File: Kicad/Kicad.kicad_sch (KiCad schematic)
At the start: 6 parts, among them J1 Screw_Terminal_01x02, J2 Screw_Terminal_01x02, J3 Screw_Terminal_01x04, U1 ESP32-WROOM-32, U2 DRV8833PW

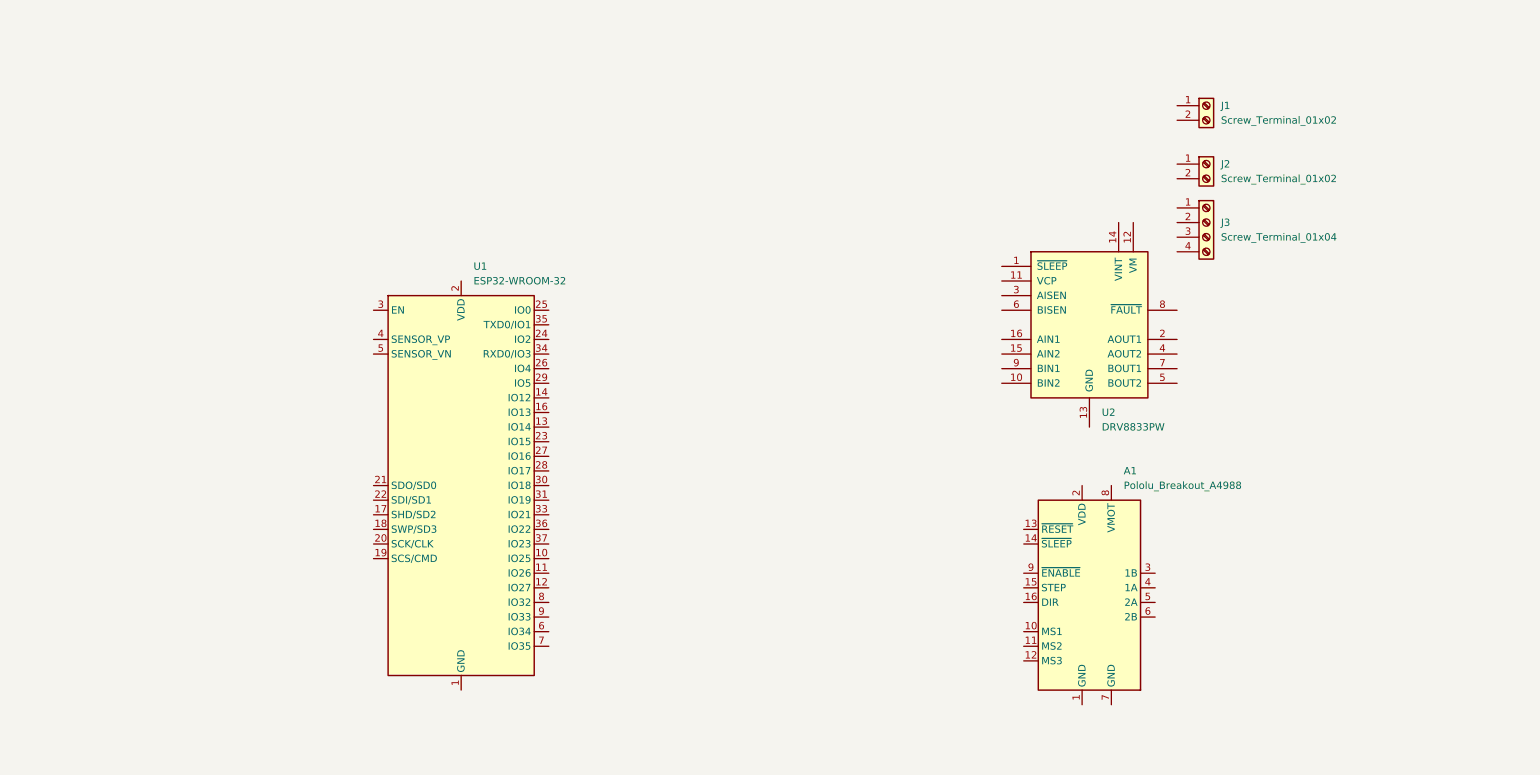
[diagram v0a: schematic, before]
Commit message: Added Power Board
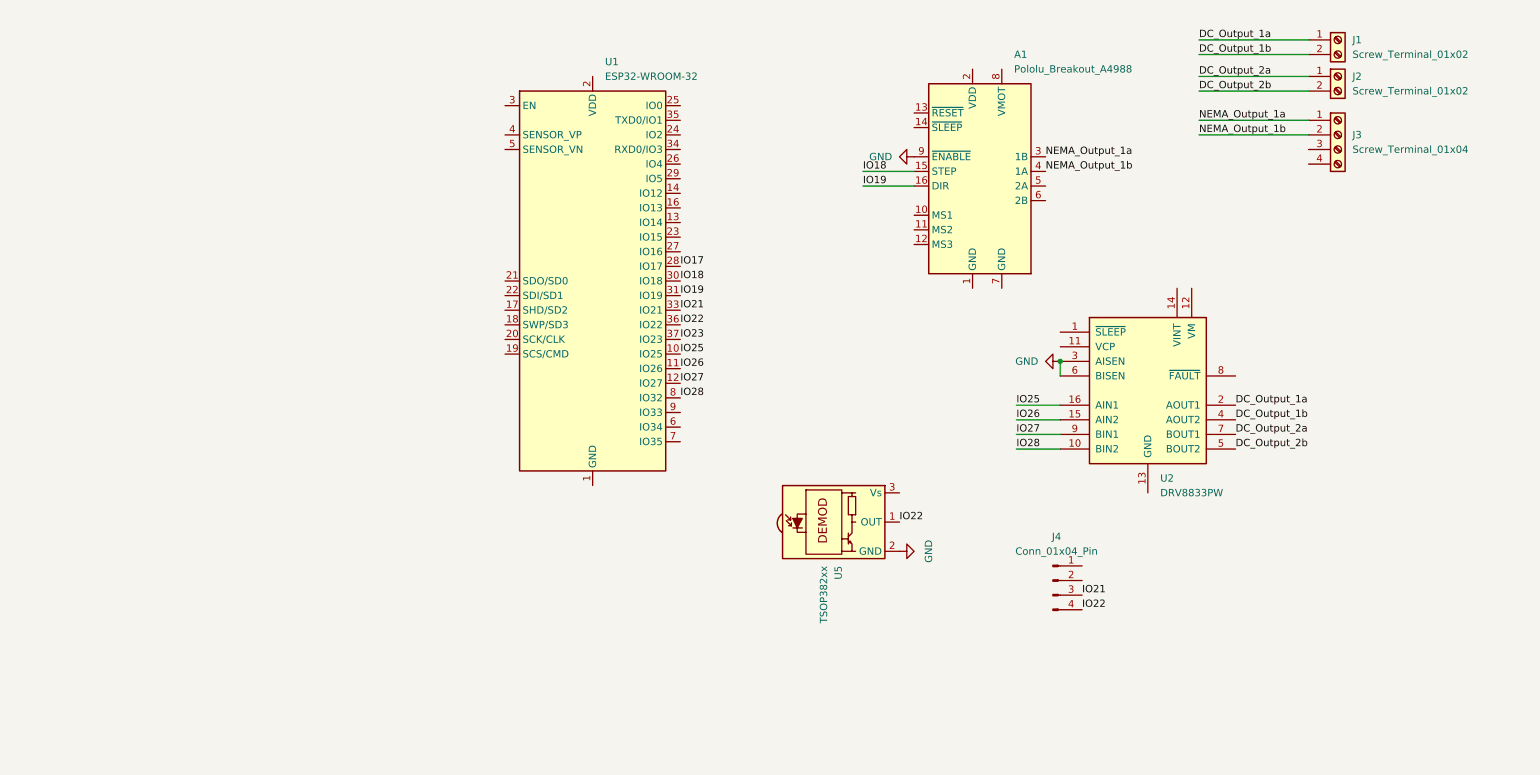
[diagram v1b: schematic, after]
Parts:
- added J4: Conn_01x04_Pin, Connector_PinHeader_2.54mm:PinHeader_1x04_P2.54mm_Vertical, symbol Connector:Conn_01x04_Pin
- added U5: TSOP382xx, OptoDevice:Vishay_MINICAST-3Pin, symbol Interface_Optical:TSOP382xx
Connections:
- net DC_Output_1a: now reaches J1.1 (Pin_1)
- net DC_Output_1a: now also U2.2 (AOUT1)
- net DC_Output_1b: now reaches J1.2 (Pin_2)
- net DC_Output_1b: now also U2.4 (AOUT2)
- net IO25: now reaches U1.10 (IO25)
- net IO25: now also U2.16 (AIN1)
- net IO26: now reaches U1.11 (IO26)
- net IO26: now also U2.15 (AIN2)
- net IO27: now reaches U1.12 (IO27)
- net IO27: now also U2.9 (BIN1)
- net IO17: now reaches U1.28 (IO17)
- net IO18: now reaches U1.30 (IO18)
- net IO18: now also A1.15 (STEP)
- net IO19: now reaches U1.31 (IO19)
- net IO19: now also A1.16 (DIR)
- net IO21: now reaches U1.33 (IO21)
- net IO21: now also J4.3 (Pin_3)
- net IO22: now reaches U1.36 (IO22)
- net IO22: now also J4.4 (Pin_4), U5.1 (OUT)
- net IO23: now reaches U1.37 (IO23)
- net IO28: now reaches U1.8 (IO32)
- net IO28: now also U2.10 (BIN2)
- net NEMA_Output_1a: now reaches A1.3 (1B)
- net NEMA_Output_1a: now also J3.1 (Pin_1)
- net NEMA_Output_1b: now reaches A1.4 (1A)
- net NEMA_Output_1b: now also J3.2 (Pin_2)
- net GND: now reaches A1.9 (~{ENABLE})
- net GND: now also U2.3 (AISEN), U2.6 (BISEN), U5.2 (GND)
- net DC_Output_2b: now reaches U2.5 (BOUT2)
- net DC_Output_2b: now also J2.2 (Pin_2)
- net DC_Output_2a: now reaches U2.7 (BOUT1)
- net DC_Output_2a: now also J2.1 (Pin_1)
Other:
- moved on the sheet: A1, J1, J2, J3, U1, U2

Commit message: Updated schematic for main board
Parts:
- added C1, C5: 10u, Capacitor_SMD:C_0603_1608Metric, symbol Device:C
- added C2, C3: 0.1u, Capacitor_SMD:C_0603_1608Metric, symbol Device:C
- added C4: 100u, Capacitor_SMD:C_0603_1608Metric, symbol Device:C
- added C6: 0.01u, Capacitor_SMD:C_0603_1608Metric, symbol Device:C
- added C7: 2.2u, Capacitor_SMD:C_0603_1608Metric, symbol Device:C
- added J5: Conn_01x04_Pin, Connector_PinHeader_2.54mm:PinHeader_1x04_P2.54mm_Vertical, symbol Connector:Conn_01x04_Pin
- added R1: 10k, Resistor_SMD:R_0603_1608Metric, symbol Device:R
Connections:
- net GND: now also A1.1 (GND), A1.7 (GND), J4.2 (Pin_2), U1.1 (GND), U1.15 (GND), U1.38 (GND), U1.39 (GND), U2.13 (GND), C1.1, C2.1, C3.1, C4.1, C5.1, C6.1, C7.1, J5.2 (Pin_2), J5.3 (Pin_3); no longer A1.9 (~{ENABLE})
- net IO23: now also A1.9 (~{ENABLE})
- net 3v3: now reaches U1.2 (VDD)
- net 3v3: now also A1.2 (VDD), J4.1 (Pin_1), U2.1 (~{SLEEP}), U2.11 (VCP), U2.12 (VM), U5.3 (Vs), C1.2, C2.2, C5.2, C6.2, J5.1 (Pin_1), R1.1
- net at U1.3 (EN): now also C3.2, R1.2
- net at A1.13 (~{RESET}): now also A1.14 (~{SLEEP})
- net NEMA_Output_2a: now reaches A1.5 (2A)
- net NEMA_Output_2a: now also J3.3 (Pin_3)
- net NEMA_Output_2b: now reaches A1.6 (2B)
- net NEMA_Output_2b: now also J3.4 (Pin_4)
- net 12V: now reaches A1.8 (VMOT)
- net 12V: now also C4.2, J5.4 (Pin_4)
- net at U2.14 (VINT): now also C7.2
- net IO17: no longer names the net of U1.28 (IO17)
- no-connect marks 0 -> 27
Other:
- moved on the sheet: U1

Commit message: Main Board v1
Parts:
- removed U1: ESP32-WROOM-32, RF_Module:ESP32-WROOM-32, symbol RF_Module:ESP32-WROOM-32
- added U3: ~, ESP32_Footprints:ESP32_30pin, symbol esp32_30pin:ESP32_30Pin
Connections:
- net 3v3: now also U3.16 (3.3v)
- net GND: now also C3.2, U3.17 (GND), U3.2 (GND); no longer C3.1
- net IO18: now also U3.3 (GPIO13)
- net IO19: now also U3.4 (GPIO12)
- net IO21: now also U3.29 (GPIO22)
- net IO22: now also U3.30 (GPIO23); no longer U5.1 (OUT)
- net IO23: now also U3.7 (GPIO26)
- net IO25: now also U2.9 (BIN1), U3.8 (GPIO25); no longer U2.16 (AIN1)
- net IO26: now also U2.10 (BIN2), U3.9 (GPIO33); no longer U2.15 (AIN2)
- net IO27: now also U2.15 (AIN2), U3.10 (GPIO32); no longer U2.9 (BIN1)
- net IO28: now also U2.16 (AIN1), U3.11 (GPIO35); no longer U2.10 (BIN2)
- net EN: now reaches R1.2
- net EN: now also C3.1, U3.15 (EN); no longer C3.2
- new net IO5: U3.23 (GPIO5), U5.1 (OUT)
- no-connect marks 27 -> 20
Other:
- moved on the sheet: C1, C2, C3, C5, C6, J5, R1

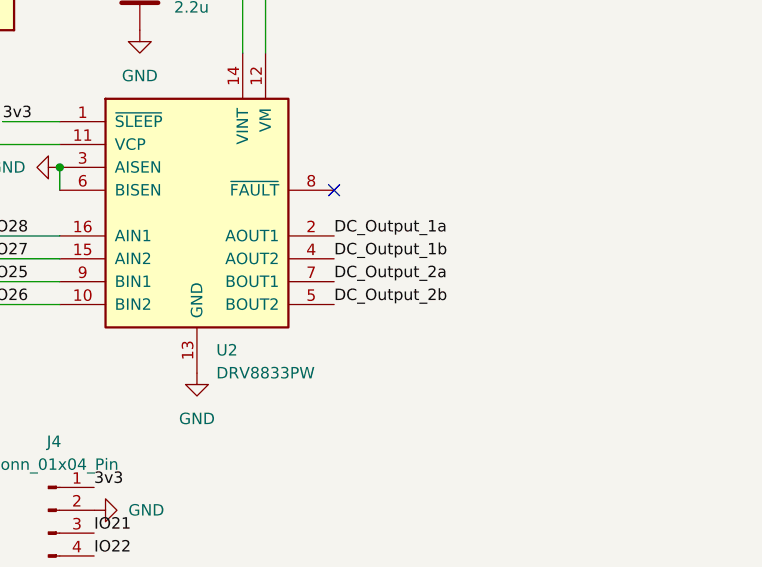
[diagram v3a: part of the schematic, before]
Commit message: Created cad for how the boards will fit together
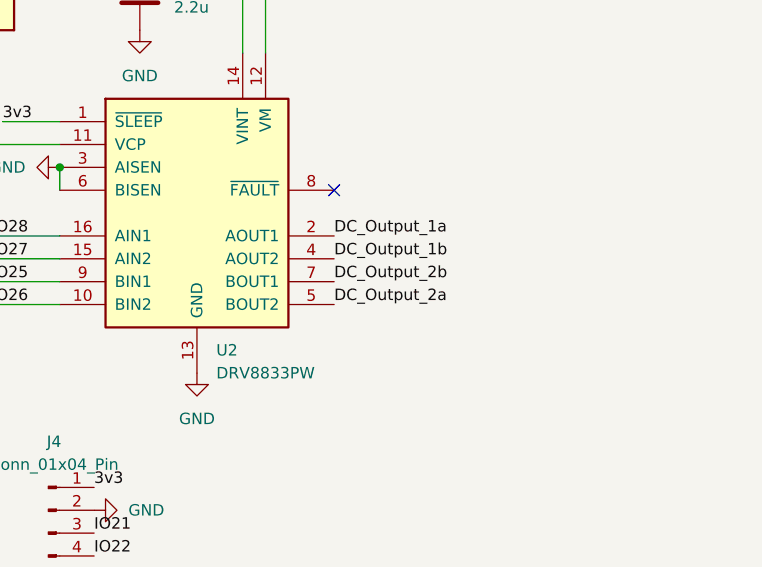
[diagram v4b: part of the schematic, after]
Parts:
- J1, J2: footprint TerminalBlock_RND:TerminalBlock_RND_205-00232_1x02_P5.08mm_Horizontal -> TerminalBlock_RND:TerminalBlock_RND_205-00045_1x02_P5.00mm_Horizontal
- J3: footprint TerminalBlock_Phoenix:TerminalBlock_Phoenix_MKDS-3-4-5.08_1x04_P5.08mm_Horizontal -> TerminalBlock_RND:TerminalBlock_RND_205-00003_1x04_P5.00mm_Horizontal
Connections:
- net DC_Output_2a: now also U2.5 (BOUT2); no longer U2.7 (BOUT1)
- net DC_Output_2b: now also U2.7 (BOUT1); no longer U2.5 (BOUT2)
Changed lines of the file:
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@@
+		)
+	)
+	(label "DC_Output_2b"
+		(at 234.95 95.25 0)
+		(effects
+			(font
+				(size 1.27 1.27)
+			)
+			(justify left bottom)
 		)
 	)
@@
 		)
 	)
-	(label "DC_Output_2b"
-		(at 234.95 97.79 0)
-		(effects
-			(font
-				(size 1.27 1.27)
-			)
-			(justify left bottom)
-		)
-	)
 	(label "3v3"
 		(at 198.12 77.47 0)
@@
 		)
 	)
-	(label "DC_Output_2a"
-		(at 234.95 95.25 0)
-		(effects
-			(font
-				(size 1.27 1.27)
-			)
-			(justify left bottom)
-		)
-	)
 	(label "IO5"
 		(at 176.53 110.49 0)
@@
 		)
 	)
+	(label "DC_Output_2a"
+		(at 234.95 97.79 0)
+		(effects
+			(font
+				(size 1.27 1.27)
+			)
+			(justify left bottom)
+		)
+	)
 	(label "3v3"
 		(at 87.63 43.18 0)
@@
 			)
 		)
-		(property "Footprint" "TerminalBlock_RND:TerminalBlock_RND_205-00232_1x02_P5.08mm_Horizontal"
+		(property "Footprint" "TerminalBlock_RND:TerminalBlock_RND_205-00045_1x02_P5.00mm_Horizontal"
 			(at 252.73 26.67 0)
 			(effects
@@
 			)
 		)
-		(property "Footprint" "TerminalBlock_RND:TerminalBlock_RND_205-00232_1x02_P5.08mm_Horizontal"
+		(property "Footprint" "TerminalBlock_RND:TerminalBlock_RND_205-00045_1x02_P5.00mm_Horizontal"
 			(at 252.73 33.02 0)
 			(effects
@@
 			)
 		)
-		(property "Footprint" "TerminalBlock_Phoenix:TerminalBlock_Phoenix_MKDS-3-4-5.08_1x04_P5.08mm_Horizontal"
+		(property "Footprint" "TerminalBlock_RND:TerminalBlock_RND_205-00003_1x04_P5.00mm_Horizontal"
 			(at 252.73 43.18 0)
 			(effects

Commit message: Wrote v1 of the code, final version of boards
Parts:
- C1, C5: value 10u -> 10uF; footprint Capacitor_SMD:C_0603_1608Metric -> PCM_JLCPCB:C_0603; symbol Device:C -> PCM_JLCPCB-Capacitors:0603,10uF; Attrition Qty (none) -> 10; Capacitance (none) -> 10uF; Category (none) -> Capacitors,Multilayer Ceramic Capacitors MLCC - SMD/SMT; Class (none) -> Basic Component; LCSC (none) -> C19702; Manufacturer (none) -> Samsung Electro-Mechanics; Minimum Qty (none) -> 20; Part (none) -> CL10A106KP8NNNC; Price (none) -> 0.009USD; Process (none) -> SMT; Stock (none) -> 9881407; Temperature Coefficient (none) -> X5R; Tolerance (none) -> ±10%; Voltage Rated (none) -> 10V
- C2, C3: value 0.1u -> 100nF; footprint Capacitor_SMD:C_0603_1608Metric -> PCM_JLCPCB:C_0603; symbol Device:C -> PCM_JLCPCB-Capacitors:0603,100nF; Attrition Qty (none) -> 10; Capacitance (none) -> 100nF; Category (none) -> Capacitors,Multilayer Ceramic Capacitors MLCC - SMD/SMT; Class (none) -> Basic Component; LCSC (none) -> C14663; Manufacturer (none) -> YAGEO; Minimum Qty (none) -> 20; Part (none) -> CC0603KRX7R9BB104; Price (none) -> 0.006USD; Process (none) -> SMT; Stock (none) -> 70324515; Temperature Coefficient (none) -> X7R; Tolerance (none) -> ±10%; Voltage Rated (none) -> 50V
- C4: footprint Capacitor_SMD:C_0603_1608Metric -> Capacitor_THT:C_Radial_D8.0mm_H11.5mm_P3.50mm
- C6: value 0.01u -> 10nF; footprint Capacitor_SMD:C_0603_1608Metric -> PCM_JLCPCB:C_0603; symbol Device:C -> PCM_JLCPCB-Capacitors:0603,10nF; Attrition Qty (none) -> 10; Capacitance (none) -> 10nF; Category (none) -> Capacitors,Multilayer Ceramic Capacitors MLCC - SMD/SMT; Class (none) -> Basic Component; LCSC (none) -> C57112; Manufacturer (none) -> FH(Guangdong Fenghua Advanced Tech); Minimum Qty (none) -> 20; Part (none) -> 0603B103K500NT; Price (none) -> 0.005USD; Process (none) -> SMT; Stock (none) -> 5921160; Temperature Coefficient (none) -> X7R; Tolerance (none) -> ±10%; Voltage Rated (none) -> 50V
- C7: value 2.2u -> 2.2uF; footprint Capacitor_SMD:C_0603_1608Metric -> PCM_JLCPCB:C_0603; symbol Device:C -> PCM_JLCPCB-Capacitors:0603,2.2uF; Attrition Qty (none) -> 10; Capacitance (none) -> 2.2uF; Category (none) -> Capacitors,Multilayer Ceramic Capacitors MLCC - SMD/SMT; Class (none) -> Basic Component; LCSC (none) -> C23630; Manufacturer (none) -> Samsung Electro-Mechanics; Minimum Qty (none) -> 20; Part (none) -> CL10A225KO8NNNC; Price (none) -> 0.009USD; Process (none) -> SMT; Stock (none) -> 2585089; Temperature Coefficient (none) -> X5R; Tolerance (none) -> ±10%; Voltage Rated (none) -> 16V
- R1: value 10k -> 10kΩ; footprint Resistor_SMD:R_0603_1608Metric -> PCM_JLCPCB:R_0603; symbol Device:R -> PCM_JLCPCB-Resistors:0603,10kΩ; Attrition Qty (none) -> 10; Category (none) -> Resistors,Chip Resistor - Surface Mount; Class (none) -> Basic Component; LCSC (none) -> C25804; Manufacturer (none) -> UNI-ROYAL(Uniroyal Elec); Minimum Qty (none) -> 20; Operating Temperature Range (none) -> -55°C~+155°C; Overload Voltage (Max) (none) -> 75V; Part (none) -> 0603WAF1002T5E; Power(Watts) (none) -> 100mW; Price (none) -> 0.004USD; Process (none) -> SMT; Resistance (none) -> 10kΩ; Stock (none) -> 51181774; Temperature Coefficient (none) -> ±100ppm/°C; Tolerance (none) -> ±1%; Type (none) -> Thick Film Resistors
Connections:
- net IO23: now also U3.6 (GPIO27); no longer U3.7 (GPIO26)
- net IO25: now also U3.7 (GPIO26); no longer U3.8 (GPIO25)
- net IO26: now also U3.8 (GPIO25); no longer U3.9 (GPIO33)
- net IO27: now also U3.9 (GPIO33); no longer U3.10 (GPIO32)
- net IO28: now also U3.10 (GPIO32); no longer U3.11 (GPIO35)

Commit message: Updated to use 0805 instead of JLC assembly
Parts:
- C1, C2, C3, C5, C6, C7: footprint PCM_JLCPCB:C_0603 -> Capacitor_SMD:C_0805_2012Metric_Pad1.18x1.45mm_HandSolder
- R1: footprint PCM_JLCPCB:R_0603 -> Resistor_SMD:R_0805_2012Metric_Pad1.20x1.40mm_HandSolder
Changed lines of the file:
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@@
 			)
 		)
-		(property "Footprint" "PCM_JLCPCB:C_0603"
+		(property "Footprint" "Capacitor_SMD:C_0805_2012Metric_Pad1.18x1.45mm_HandSolder"
 			(at 163.068 83.82 90)
 			(effects
@@
 			)
 		)
-		(property "Footprint" "PCM_JLCPCB:C_0603"
+		(property "Footprint" "Capacitor_SMD:C_0805_2012Metric_Pad1.18x1.45mm_HandSolder"
 			(at 129.032 132.08 90)
 			(effects
@@
 			)
 		)
-		(property "Footprint" "PCM_JLCPCB:C_0603"
+		(property "Footprint" "Capacitor_SMD:C_0805_2012Metric_Pad1.18x1.45mm_HandSolder"
 			(at 169.418 83.82 90)
 			(effects
@@
 			)
 		)
-		(property "Footprint" "PCM_JLCPCB:C_0603"
+		(property "Footprint" "Capacitor_SMD:C_0805_2012Metric_Pad1.18x1.45mm_HandSolder"
 			(at 81.788 90.17 90)
 			(effects
@@
 			)
 		)
-		(property "Footprint" "PCM_JLCPCB:C_0603"
+		(property "Footprint" "Capacitor_SMD:C_0805_2012Metric_Pad1.18x1.45mm_HandSolder"
 			(at 215.138 63.5 90)
 			(effects
@@
 			)
 		)
-		(property "Footprint" "PCM_JLCPCB:R_0603"
+		(property "Footprint" "Resistor_SMD:R_0805_2012Metric_Pad1.20x1.40mm_HandSolder"
 			(at 140.97 120.142 90)
 			(effects
@@
 			)
 		)
-		(property "Footprint" "PCM_JLCPCB:C_0603"
+		(property "Footprint" "Capacitor_SMD:C_0805_2012Metric_Pad1.18x1.45mm_HandSolder"
 			(at 72.898 90.17 90)
 			(effects
